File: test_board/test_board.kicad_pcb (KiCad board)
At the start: 4 copper layers, 98.9 x 68.2 mm, 164 parts, among them J1 Conn_01x24_Socket, J2 Conn_01x24_Socket, SW1 CJS-1201B, U1 TLV3601DCKR, U10 TLV3601DCKR, U11 TLV3601DCKR, U12 TLV3601DCKR, U14 REF3012, U15 REF3025, U3 TLV3601DCKR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

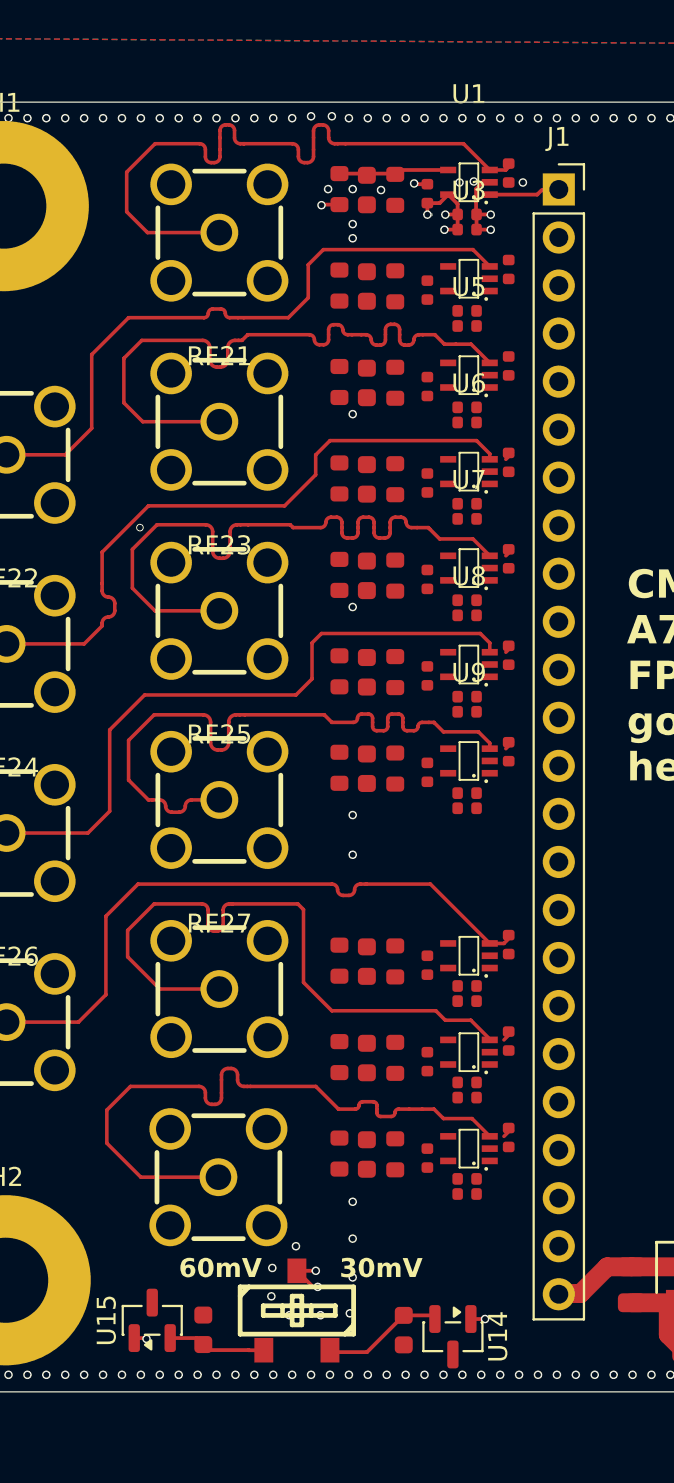
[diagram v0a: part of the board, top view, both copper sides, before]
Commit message: added uart connector
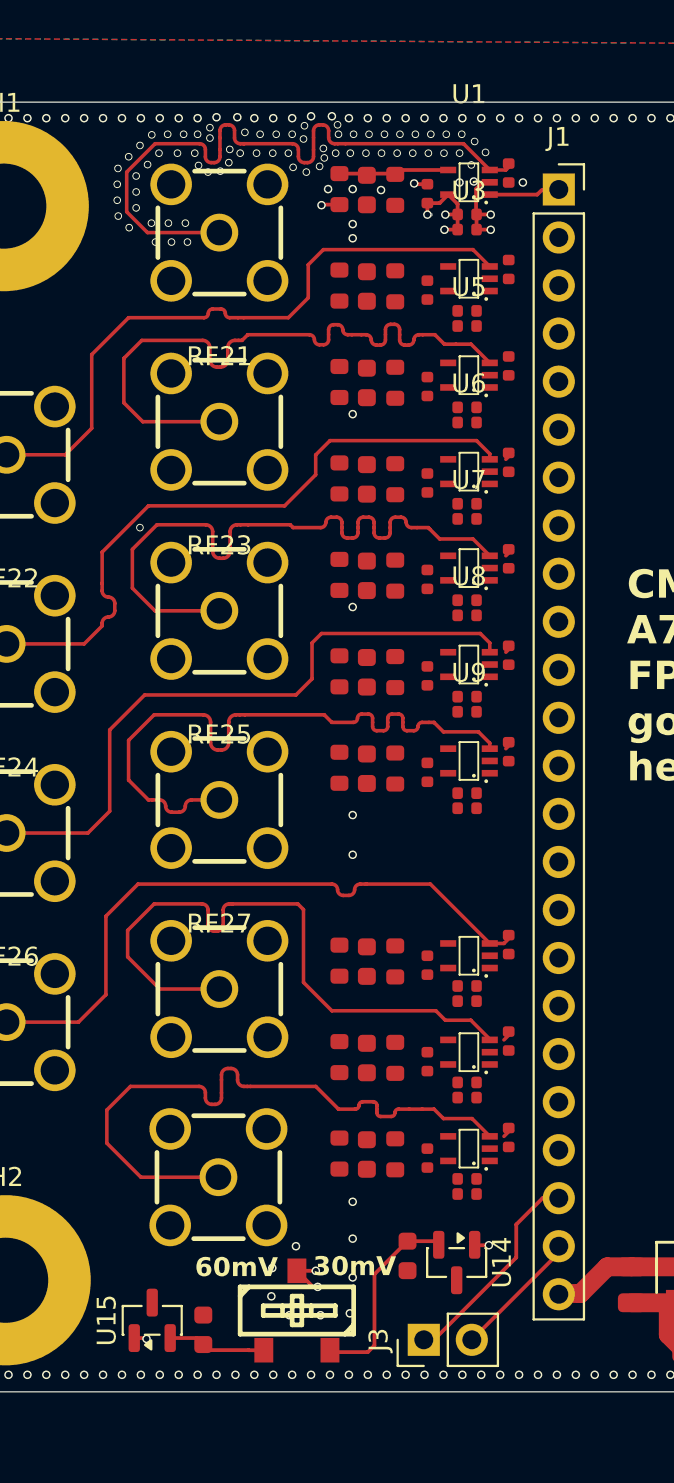
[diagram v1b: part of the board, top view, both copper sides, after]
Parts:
- added J3: Conn_01x02_Pin, Connector_PinHeader_2.54mm:PinHeader_1x02_P2.54mm_Vertical, F.Cu at (74.6, 99.5)
- moved C43 3.93 mm to (73.8, 95.0)
- moved U14 3.93 mm to (76.3, 95.4)
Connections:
- J1 pad 22: unconnected-(J1-Pin_22-Pad22) -> pin22
- J1 pad 23: unconnected-(J1-Pin_23-Pad23) -> pin23
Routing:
- net pin22: track 0.00 -> 11.3 mm
- net pin23: track 0.00 -> 6.86 mm
- net Net-(U14-OUT): track 6.48 -> 10.5 mm
- net GND: vias 344 -> 412

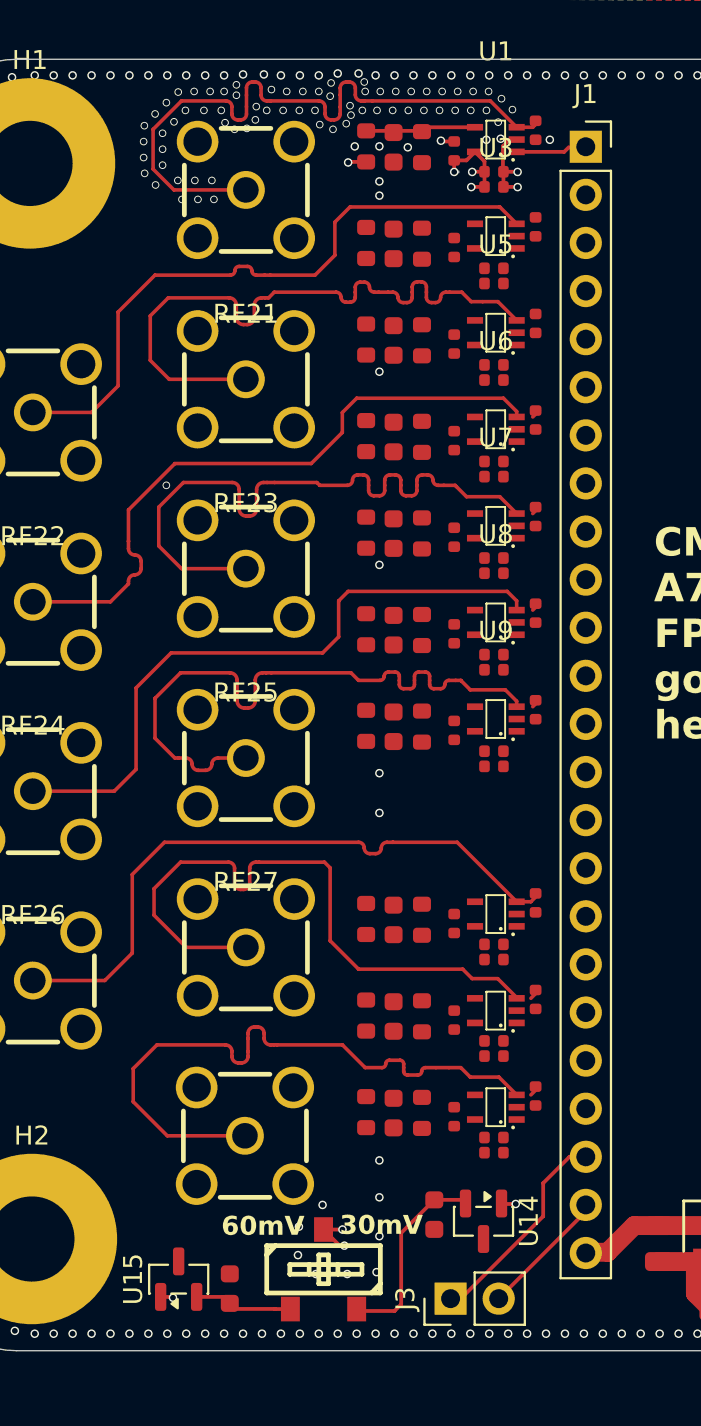
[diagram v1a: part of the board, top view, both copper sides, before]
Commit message: added decoupling caps to regulator and changed comparator termination resistor to 49.9 ohm
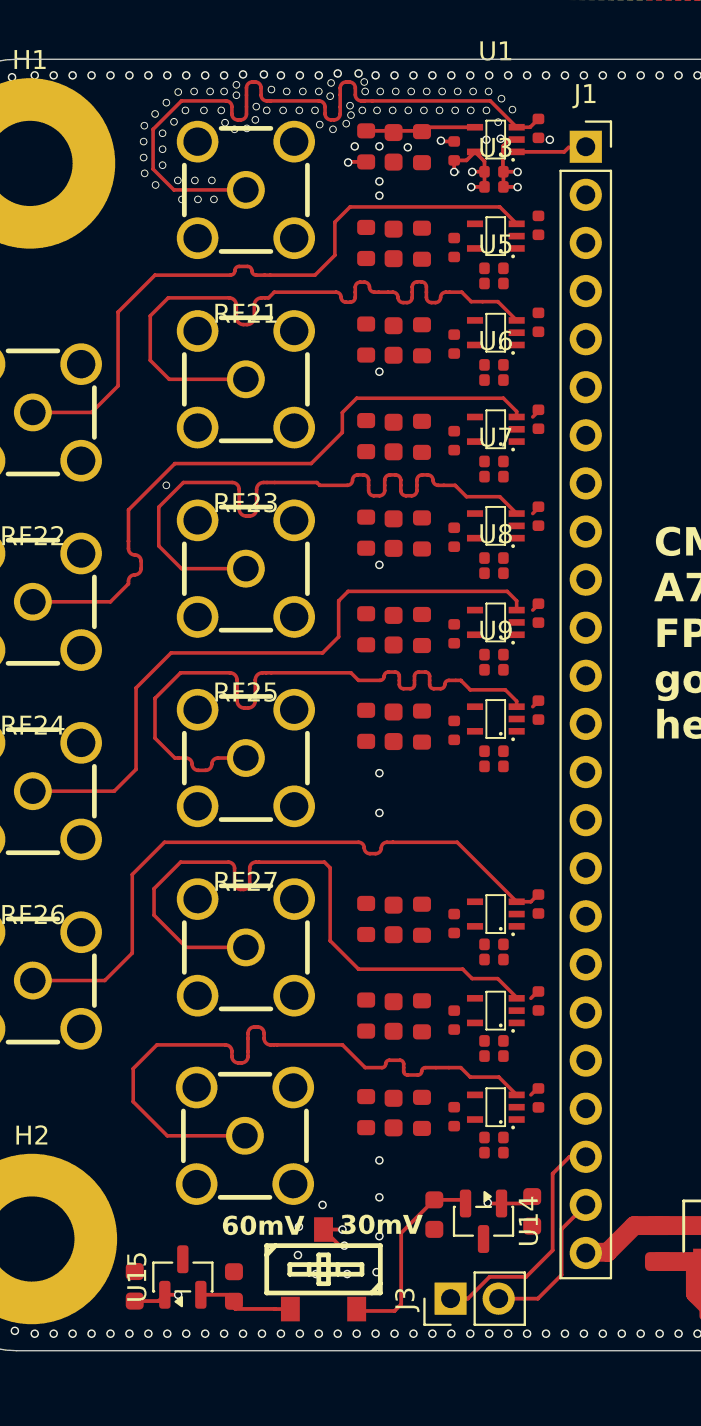
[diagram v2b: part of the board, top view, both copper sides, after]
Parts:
- removed R71, R72, R73, R74, R75, R76, R77, R78, R79, R80: 51Ω, PCM_JLCPCB:R_0402
- added C45: 220nF, PCM_JLCPCB:C_0603, F.Cu at (57.9, 98.8)
- added C46: 220nF, PCM_JLCPCB:C_0603, F.Cu at (78.9, 94.8)
- added R41: 49.9Ω, PCM_JLCPCB:R_0402, F.Cu at (79.2, 37.6)
- added R42: 49.9Ω, PCM_JLCPCB:R_0402, F.Cu at (79.2, 42.8)
- added R45: 49.9Ω, PCM_JLCPCB:R_0402, F.Cu at (79.2, 47.9)
- added R47: 49.9Ω, PCM_JLCPCB:R_0402, F.Cu at (79.2, 53.0)
- added R49: 49.9Ω, PCM_JLCPCB:R_0402, F.Cu at (79.2, 58.1)
- added R51: 49.9Ω, PCM_JLCPCB:R_0402, F.Cu at (79.2, 63.2)
- added R53: 49.9Ω, PCM_JLCPCB:R_0402, F.Cu at (79.2, 68.4)
- added R55: 49.9Ω, PCM_JLCPCB:R_0402, F.Cu at (79.2, 78.6)
- added R57: 49.9Ω, PCM_JLCPCB:R_0402, F.Cu at (79.2, 83.7)
- added R59: 49.9Ω, PCM_JLCPCB:R_0402, F.Cu at (79.2, 88.8)
- moved C44 0.25 mm to (63.2, 98.8)
- moved U15 0.25 mm to (60.5, 98.3)
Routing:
- net +3.3V: track 11.2 -> 14.7 mm
- net pin22: track 11.3 -> 12.6 mm
- net pin23: track 6.86 -> 8.07 mm

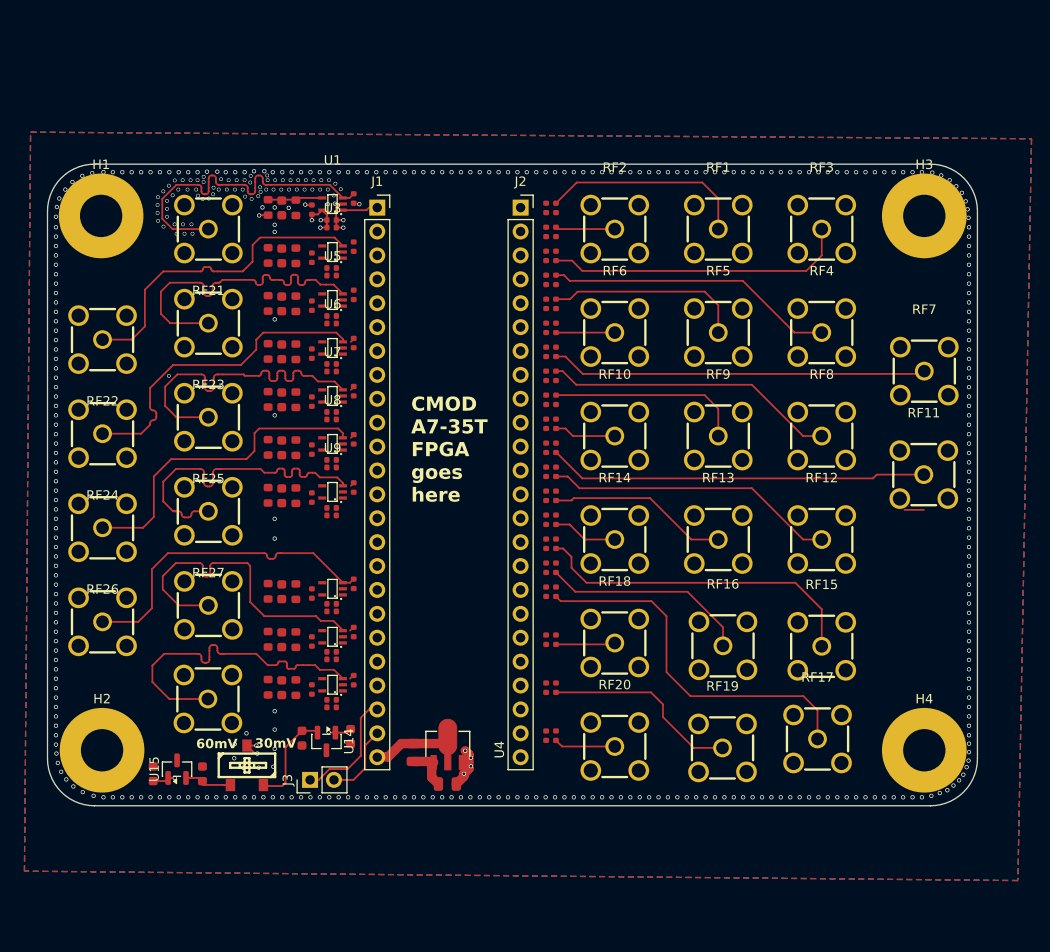
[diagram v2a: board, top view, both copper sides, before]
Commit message: spaced out SMA connectors
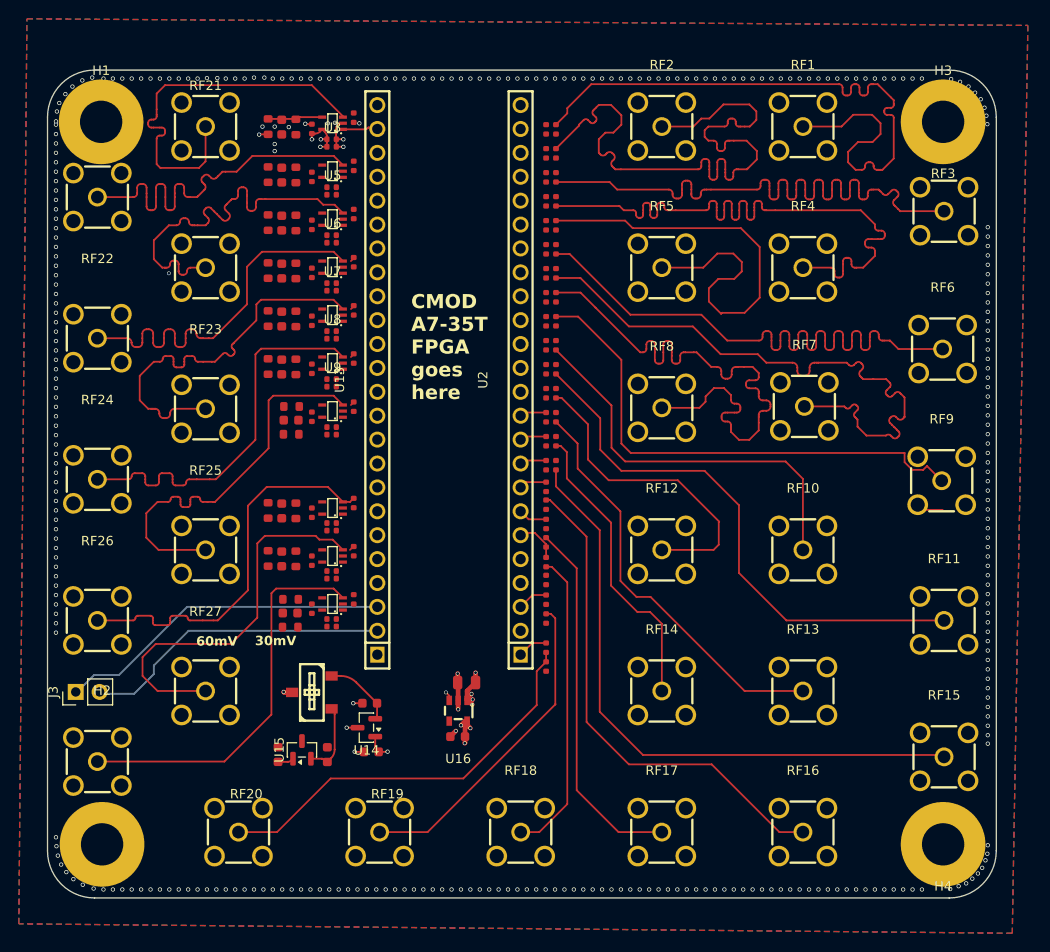
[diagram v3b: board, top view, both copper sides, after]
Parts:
- removed J1, J2: Conn_01x24_Socket, Connector_PinSocket_2.54mm:PinSocket_1x24_P2.54mm_Vertical
- removed U4: HT7533-1_C14289, easyeda2kicad:SOT-89-3_L4.5-W2.5-P1.50-LS4.2-BR
- added U13: HC-PM254-8.5H-1X24PZ, easyeda2kicad:HDR-TH_24P-P2.54-V-F, F.Cu at (81.8, 56.9)
- added U16: TLV75733PDBVR, easyeda2kicad:SOT-23-5_L2.9-W1.6-P0.95-LS2.8-BL, F.Cu at (90.3, 92.1)
- added U2: HC-PM254-8.5H-1X24PZ, easyeda2kicad:HDR-TH_24P-P2.54-V-F, F.Cu at (97.0, 56.9)
- C12: value 10uF -> 2.2uF; footprint PCM_JLCPCB:C_0805 -> PCM_JLCPCB:C_0603
- moved RF20 41.0 mm to (67.0, 105.0)
- moved RF19 37.5 mm to (82.0, 105.0)
- moved RF6 34.9 mm to (141.8, 53.6)
- moved J3 26.6 mm to (49.7, 90.1)
- moved RF9 24.2 mm to (141.8, 67.7)
- moved RF10 23.4 mm to (127.0, 75.0)
- moved RF18 22.5 mm to (97.0, 105.0)
- moved RF16 21.5 mm to (127.0, 105.0)
- moved RF17 19.3 mm to (112.0, 105.0)
- moved RF13 18.4 mm to (127.0, 90.0)
- moved RF15 17.5 mm to (142.0, 97.0)
- moved RF8 17.3 mm to (112.0, 59.9)
- moved RF12 17.0 mm to (112.0, 75.0)
- moved RF14 16.9 mm to (112.0, 90.0)
- moved RF11 15.6 mm to (142.0, 82.5)
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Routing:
- net /out1/50m_out: track 6.33 -> 71.6 mm
- net /out5/50m_out: track 6.25 -> 66.3 mm
- net /out0/50m_out: track 22.1 -> 72.0 mm
- net /out3/50m_out: track 30.8 -> 69.2 mm
- net /out2/50m_out: track 32.2 -> 69.1 mm
- net /out19/50m_out: track 6.52 -> 43.3 mm
- net /out9/50m_out: track 6.58 -> 42.1 mm
- net /out8/50m_out: track 20.8 -> 54.4 mm
- net /out7/50m_out: track 31.1 -> 64.1 mm
- net /out15/50m_out: track 22.1 -> 53.5 mm
- net /out14/50m_out: track 35.5 -> 66.2 mm
- net /out4/50m_out: track 21.1 -> 51.0 mm
- net /out6/50m_out: track 39.5 -> 66.9 mm
- net /out17/50m_out: track 6.31 -> 32.7 mm
- net /out13/50m_out: track 6.91 -> 31.8 mm
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- added copper zone on In2.Cu, net +5V
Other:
- board size 98.9 x 68.2 mm -> 100.9 x 88 mm

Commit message: finished routing just need to add fencing vias
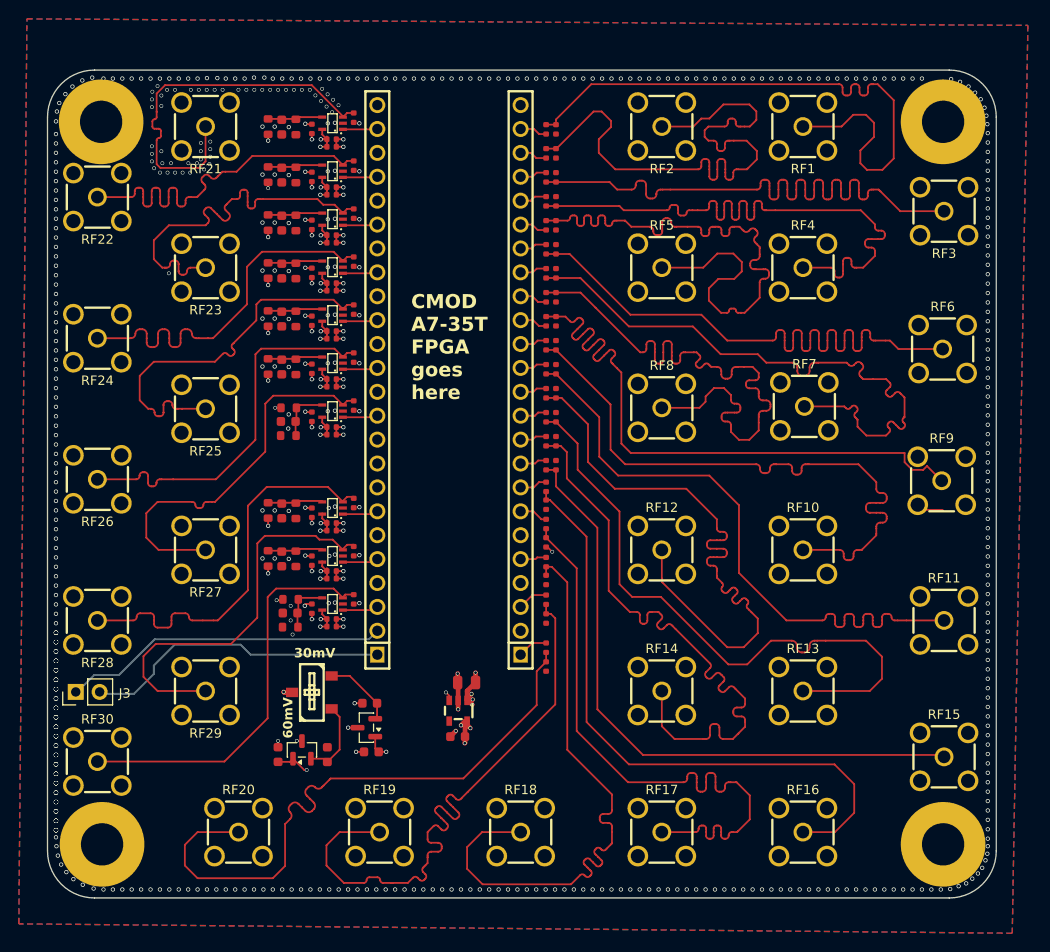
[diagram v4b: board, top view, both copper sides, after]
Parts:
- moved C39 0.33 mm to (72.3, 61.4)
- moved R54 0.33 mm to (72.3, 59.9)
- moved R67 0.33 mm to (72.3, 62.9)
- moved R53 0.12 mm to (79.2, 59.7)
- moved R51 0.10 mm to (79.2, 54.6)
- moved R49 0.08 mm to (79.2, 49.5)
- moved R47 0.06 mm to (79.2, 44.4)
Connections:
- R17 pad 1: /out8/3.3out -> out8
- U13 pad 11: unconnected-(U13-Pad11) -> in6
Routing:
- net +3.3V: track 14.6 -> 60.0 mm, vias 7 -> 35
- net /out13/50m_out: track 31.8 -> 66.8 mm
- net /out17/50m_out: track 32.7 -> 66.9 mm
- net /out11/50m_out: track 33.7 -> 66.9 mm
- net /out18/50m_out: track 34.7 -> 66.8 mm
- net /out16/50m_out: track 39.1 -> 66.8 mm
- net GND: track 15.1 -> 42.4 mm, vias 337 -> 601
- net /out9/50m_out: track 42.1 -> 66.8 mm
- net /out19/50m_out: track 43.3 -> 67.0 mm
- net /out12/50m_out: track 44.0 -> 67.1 mm
- net /out4/50m_out: track 51.0 -> 66.6 mm
- net /out15/50m_out: track 53.5 -> 67.0 mm
- net /out8/50m_out: track 54.4 -> 66.9 mm
- net /out10/50m_out: track 58.3 -> 67.0 mm
- net vref: track 1.88 -> 7.95 mm, vias 2 -> 11
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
